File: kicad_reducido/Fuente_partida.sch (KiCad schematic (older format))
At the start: 4 parts

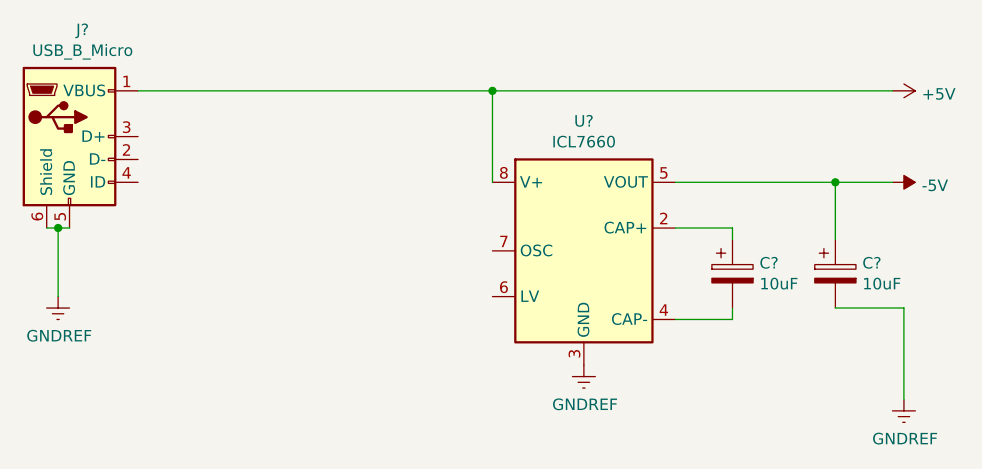
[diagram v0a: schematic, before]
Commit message: agregar pdfs actualizados y achichar esquematico fuente para paper
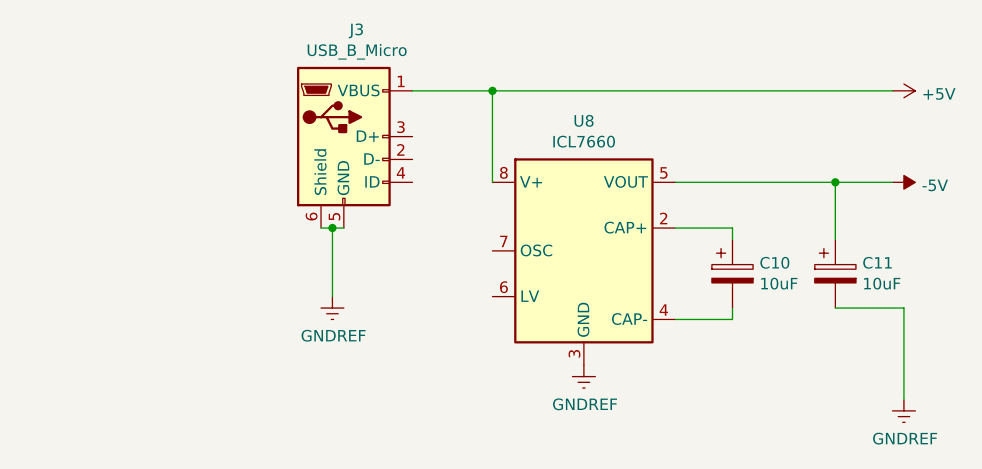
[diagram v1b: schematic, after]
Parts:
- gave numbers to parts that had none: 4
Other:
- moved on the sheet: J3
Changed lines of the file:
@@
 $Descr A4 11693 8268
 encoding utf-8
-Sheet 1 1
+Sheet 4 4
 Title ""
 Date ""
@@
 $EndDescr
 $Comp
-L Regulator_SwitchedCapacitor:ICL7660 U?
+L Regulator_SwitchedCapacitor:ICL7660 U8
 U 1 1 61FEE6DB
 P 5250 3300
-F 0 "U?" H 5250 3867 50  0000 C CNN
+F 0 "U8" H 5250 3867 50  0000 C CNN
 F 1 "ICL7660" H 5250 3776 50  0000 C CNN
 F 2 "" H 5350 3200 50  0001 C CNN
@@
 L power:GNDREF #PWR?
 U 1 1 61FF03CE
-P 2950 3500
-F 0 "#PWR?" H 2950 3250 50  0001 C CNN
-F 1 "GNDREF" H 2955 3327 50  0000 C CNN
-F 2 "" H 2950 3500 50  0001 C CNN
-F 3 "" H 2950 3500 50  0001 C CNN
-	1    2950 3500
+P 4150 3500
+F 0 "#PWR?" H 4150 3250 50  0001 C CNN
+F 1 "GNDREF" H 4155 3327 50  0000 C CNN
+F 2 "" H 4150 3500 50  0001 C CNN
+F 3 "" H 4150 3500 50  0001 C CNN
+	1    4150 3500
 	1    0    0    -1
 $EndComp
 $Comp
-L Device:CP C?
+L Device:CP C10
 U 1 1 61FF1C90
 P 5900 3400
-F 0 "C?" H 6018 3446 50  0000 L CNN
+F 0 "C10" H 6018 3446 50  0000 L CNN
 F 1 "10uF" H 6018 3355 50  0000 L CNN
 F 2 "" H 5938 3250 50  0001 C CNN
@@
 $EndComp
 Wire Wire Line
-	3300 2600 4850 2600
+	4500 2600 4850 2600
 Wire Wire Line
 	4850 3000 4850 2600
 Connection ~ 4850 2600
-Wire Wire Line
-	4850 2600 6600 2600
 $Comp
-L Device:CP C?
+L Device:CP C11
 U 1 1 61FF5FA6
 P 6350 3400
-F 0 "C?" H 6468 3446 50  0000 L CNN
+F 0 "C11" H 6468 3446 50  0000 L CNN
 F 1 "10uF" H 6468 3355 50  0000 L CNN
 F 2 "" H 6388 3250 50  0001 C CNN
@@
 Connection ~ 6350 3000
 $Comp
-L Connector:USB_B_Micro J?
+L Connector:USB_B_Micro J3
 U 1 1 61FEEB78
-P 3000 2800
-F 0 "J?" H 3057 3267 50  0000 C CNN
-F 1 "USB_B_Micro" H 3057 3176 50  0000 C CNN
-F 2 "" H 3150 2750 50  0001 C CNN
-F 3 "~" H 3150 2750 50  0001 C CNN
-	1    3000 2800
+P 4200 2800
+F 0 "J3" H 4257 3267 50  0000 C CNN
+F 1 "USB_B_Micro" H 4257 3176 50  0000 C CNN
+F 2 "" H 4350 2750 50  0001 C CNN
+F 3 "~" H 4350 2750 50  0001 C CNN
+	1    4200 2800
 	1    0    0    -1
 $EndComp
 Wire Wire Line
-	2950 3500 2950 3200
+	4150 3500 4150 3200
 Wire Wire Line
-	2900 3200 2950 3200
+	4100 3200 4150 3200
 Wire Wire Line
-	2950 3200 3000 3200
-Connection ~ 2950 3200
+	4150 3200 4200 3200
+Connection ~ 4150 3200
+Wire Wire Line
+	4850 2600 6600 2600
 $EndSCHEMATC

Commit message: agregado lo de Hernan y fixeado el kicad pcb
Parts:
- renumbered C10 to C1, C11 to C2, J3 to J13, U8 to U6
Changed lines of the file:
@@
 $EndDescr
 $Comp
-L Regulator_SwitchedCapacitor:ICL7660 U8
+L Regulator_SwitchedCapacitor:ICL7660 U6
 U 1 1 61FEE6DB
 P 5250 3300
-F 0 "U8" H 5250 3867 50  0000 C CNN
+F 0 "U6" H 5250 3867 50  0000 C CNN
 F 1 "ICL7660" H 5250 3776 50  0000 C CNN
 F 2 "" H 5350 3200 50  0001 C CNN
@@
 $EndComp
 $Comp
-L power:GNDREF #PWR?
+L power:GNDREF #PWR029
 U 1 1 61FEFED8
 P 5250 3800
-F 0 "#PWR?" H 5250 3550 50  0001 C CNN
+F 0 "#PWR029" H 5250 3550 50  0001 C CNN
 F 1 "GNDREF" H 5255 3627 50  0000 C CNN
 F 2 "" H 5250 3800 50  0001 C CNN
@@
 $EndComp
 $Comp
-L power:GNDREF #PWR?
+L power:GNDREF #PWR028
 U 1 1 61FF03CE
 P 4150 3500
-F 0 "#PWR?" H 4150 3250 50  0001 C CNN
+F 0 "#PWR028" H 4150 3250 50  0001 C CNN
 F 1 "GNDREF" H 4155 3327 50  0000 C CNN
 F 2 "" H 4150 3500 50  0001 C CNN
@@
 $EndComp
 $Comp
-L Device:CP C10
+L Device:CP C1
 U 1 1 61FF1C90
 P 5900 3400
-F 0 "C10" H 6018 3446 50  0000 L CNN
+F 0 "C1" H 6018 3446 50  0000 L CNN
 F 1 "10uF" H 6018 3355 50  0000 L CNN
 F 2 "" H 5938 3250 50  0001 C CNN
@@
 	5900 3600 5900 3550
 $Comp
-L power:+5V #PWR?
+L power:+5V #PWR030
 U 1 1 61FF3A6D
 P 6600 2600
-F 0 "#PWR?" H 6600 2450 50  0001 C CNN
+F 0 "#PWR030" H 6600 2450 50  0001 C CNN
 F 1 "+5V" V 6615 2728 50  0000 L CNN
 F 2 "" H 6600 2600 50  0001 C CNN
@@
 Connection ~ 4850 2600
 $Comp
-L Device:CP C11
+L Device:CP C2
 U 1 1 61FF5FA6
 P 6350 3400
-F 0 "C11" H 6468 3446 50  0000 L CNN
+F 0 "C2" H 6468 3446 50  0000 L CNN
 F 1 "10uF" H 6468 3355 50  0000 L CNN
 F 2 "" H 6388 3250 50  0001 C CNN
@@
 	6350 3000 5650 3000
 $Comp
-L power:GNDREF #PWR?
+L power:GNDREF #PWR032
 U 1 1 61FF65C1
 P 6650 3950
-F 0 "#PWR?" H 6650 3700 50  0001 C CNN
+F 0 "#PWR032" H 6650 3700 50  0001 C CNN
 F 1 "GNDREF" H 6655 3777 50  0000 C CNN
 F 2 "" H 6650 3950 50  0001 C CNN
@@
 	6650 3550 6650 3950
 $Comp
-L power:-5V #PWR?
+L power:-5V #PWR031
 U 1 1 61FF6BA0
 P 6600 3000
-F 0 "#PWR?" H 6600 3100 50  0001 C CNN
+F 0 "#PWR031" H 6600 3100 50  0001 C CNN
 F 1 "-5V" V 6615 3128 50  0000 L CNN
 F 2 "" H 6600 3000 50  0001 C CNN
@@
 Connection ~ 6350 3000
 $Comp
-L Connector:USB_B_Micro J3
+L Connector:USB_B_Micro J13
 U 1 1 61FEEB78
 P 4200 2800
-F 0 "J3" H 4257 3267 50  0000 C CNN
+F 0 "J13" H 4257 3267 50  0000 C CNN
 F 1 "USB_B_Micro" H 4257 3176 50  0000 C CNN
 F 2 "" H 4350 2750 50  0001 C CNN
